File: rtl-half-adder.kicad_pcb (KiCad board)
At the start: 2 copper layers, 152.4 x 114.3 mm, 109 parts, among them Q1 Q_NPN_EBC, Q10 Q_NPN_EBC, Q11 Q_NPN_EBC, Q12 Q_NPN_EBC, Q13 Q_NPN_EBC, Q14 Q_NPN_EBC, Q15 Q_NPN_EBC, Q16 Q_NPN_BEC, Q17 Q_NPN_BEC, Q18 Q_NPN_BEC, Q19 Q_NPN_BEC, Q2 Q_NPN_EBC, Q3 Q_NPN_EBC, Q4 Q_NPN_EBC, Q5 Q_NPN_EBC, Q6 Q_NPN_EBC, Q7 Q_NPN_EBC, Q8 Q_NPN_EBC, Q9 Q_NPN_EBC, SW1 SW_SPDT, SW2 SW_SPDT, SW3 SW_SPDT

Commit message: fix issues with some tracks
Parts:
- removed the REF** at (86.6, 143.3)
- removed the REF** at (118.9, 145.9)
- removed the REF** at (113.0, 145.9)
- removed the REF** at (107.2, 145.9)
- added REF**: OSHW-Logo_11.4x12mm_SilkScreen, Symbol:OSHW-Logo_11.4x12mm_SilkScreen, B.Cu at (111.5, 143.0)
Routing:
- net A: track 210.4 -> 189.7 mm, vias 2 -> 0
- net XOR3: track 39.3 -> 34.3 mm
- net XOR1: track 47.6 -> 43.3 mm
- net Net-(D1-Pad1): track 47.8 -> 43.8 mm
- net XOR2: track 34.0 -> 32.0 mm
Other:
- board text added: "CC BY-NC-SA github.com/tyehle/rtl-half-adder"
- board text added: "Tobin Yehle 2019-06-12 v1"
- board text removed: "CC BY-NC-SA"
- board text removed: "Tobin Yehle 2019-06-11 v1"

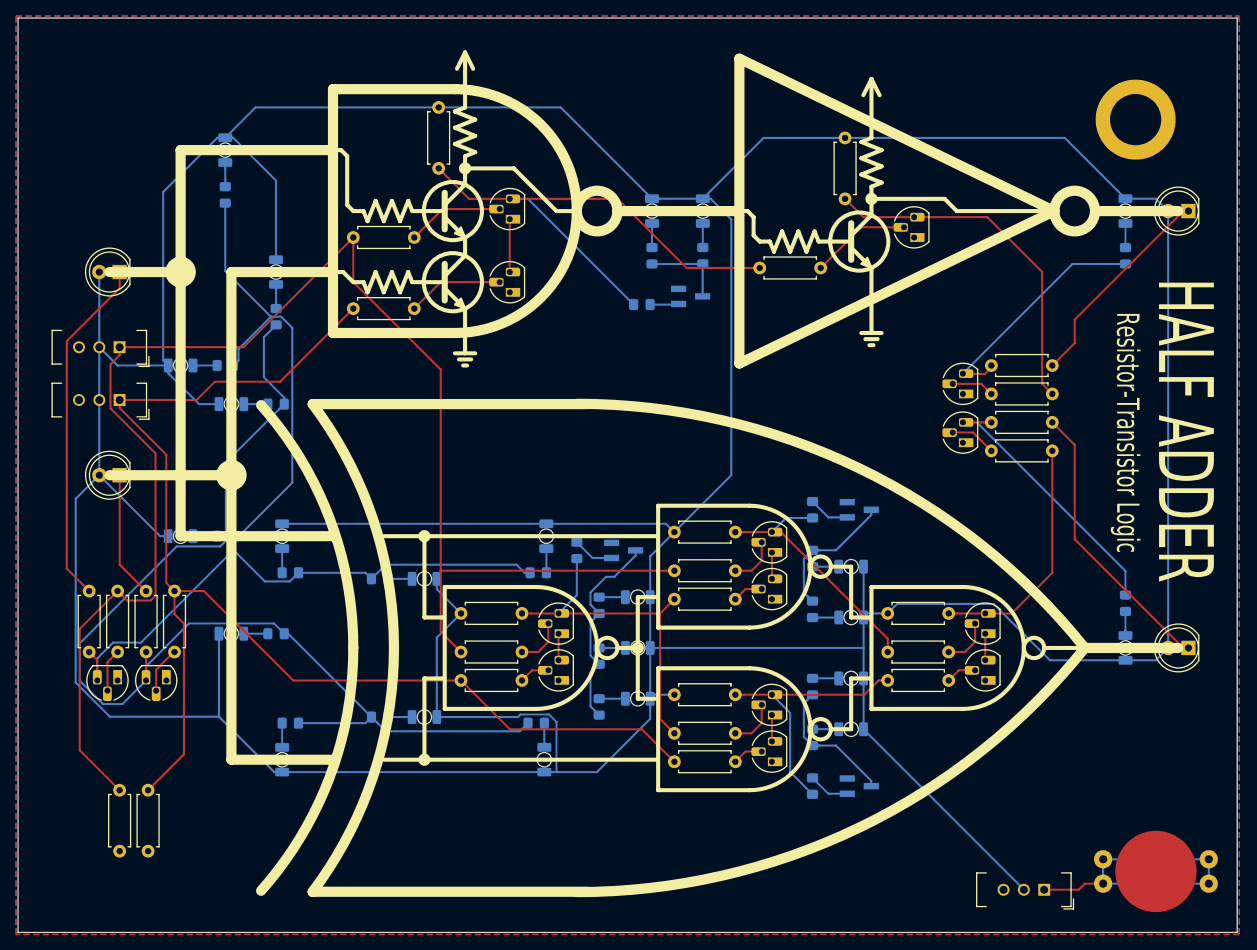
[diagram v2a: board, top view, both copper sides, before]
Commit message: change led footprint
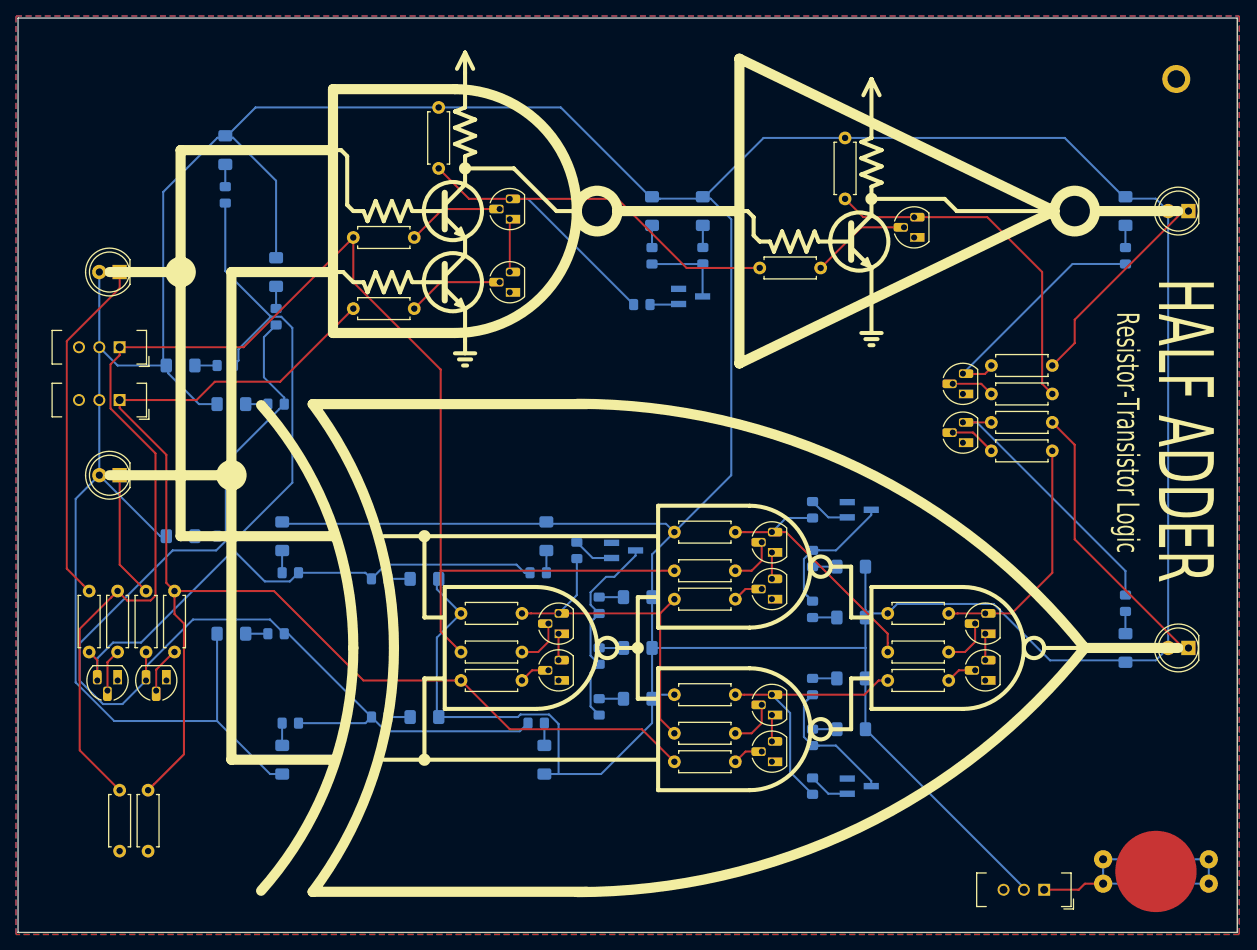
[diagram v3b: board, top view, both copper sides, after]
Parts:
- removed the REF** at (190.5, 50.8)
- added REF**: MountingHole, MountingHole:MountingHole_2.2mm_M2_ISO7380_Pad, F.Cu at (195.6, 45.7)
- D10, D11, D12, D13, D14, D15, D16, D17, D18, D19, D20, D21, D22, D23, D24, D25, D26, D27, D5, D6, D7, D8, D9: footprint --Project:LED_1206_3216Metric_ReverseMount_Hole1.8x2.4mm -> --Project:LED_1206_ReverseMountSquare1.5mm_HandSolder
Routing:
- net VCC: track 692.2 -> 660.8 mm

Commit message: update fab layer with new labels
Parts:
- D1, D2: value LED -> Red
- D10, D11, D12, D13, D14, D15, D16, D17, D18, D19, D20, D21, D22, D23, D24, D25, D26, D27, D5, D6, D7, D8, D9: value LED -> Yellow
- D3, D4: value LED -> Green
- R2, R26, R27, R29, R30, R32, R33, R34, R36, R37, R39, R4, R40, R41, R42, R43, R44, R45, R46, R47, R48, R49, R50, R51, R52, R53, R54: value 68 -> 510
